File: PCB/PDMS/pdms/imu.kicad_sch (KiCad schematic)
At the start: 1 part

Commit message: Full imu schematics
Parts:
- added C? (x2): 100nF, symbol Device:C_Small
- added C?: 10nF, symbol Device:C_Small
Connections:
- net GND: now also IC?.2 (RES_1), IC?.3 (RES_2), C?.1, C?.2, C?.2
- net IMU_I2C_SA0: now reaches IC?.1 (SDO/SA0)
- net IMU_MODE_SEL: now reaches IC?.12 (CS)
- net IMU_SCL: now reaches IC?.13 (SCL)
- net IMU_I2C_SDA: now reaches IC?.14 (SDA)
- net IMU_INT1: now reaches IC?.4 (INT1)
- net +3.3V: now reaches IC?.5 (VDDIO)
- net +3.3V: now also IC?.8 (VDD), C?.1, C?.1, C?.2
- net IMU_INT2: now reaches IC?.9 (INT2)
- no-connect marks 0 -> 2
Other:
- note added: "ASM330 - SAFETY IMU"
- moved on the sheet: IC?

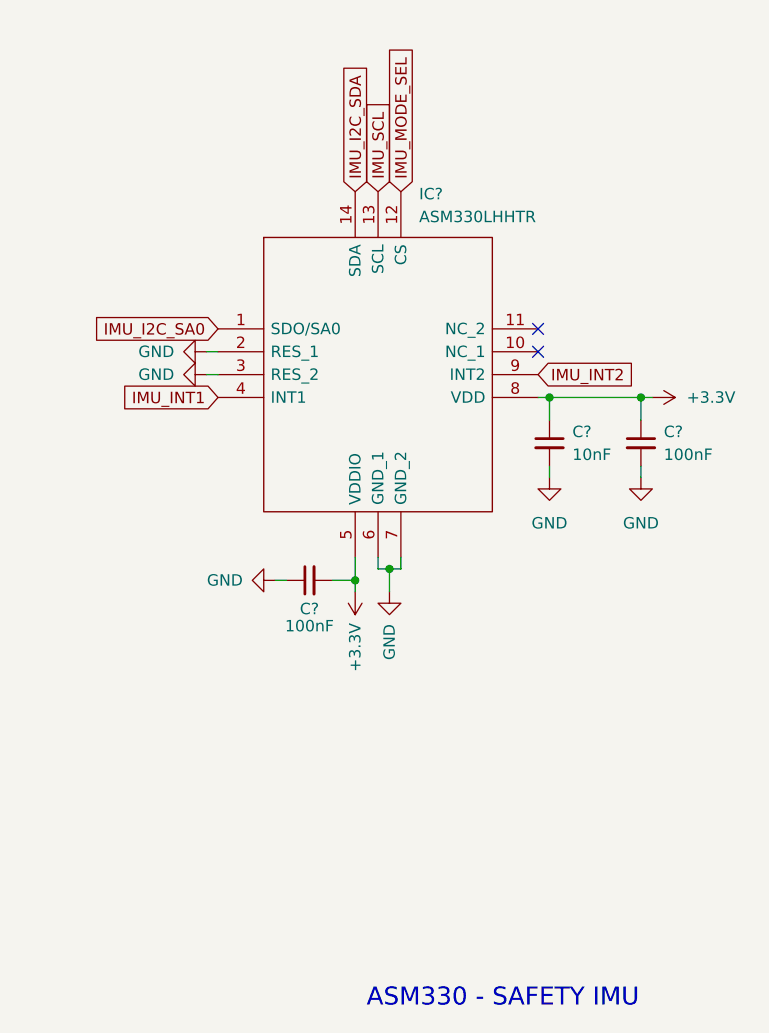
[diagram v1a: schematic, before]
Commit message: Modified power switch section - partly finished
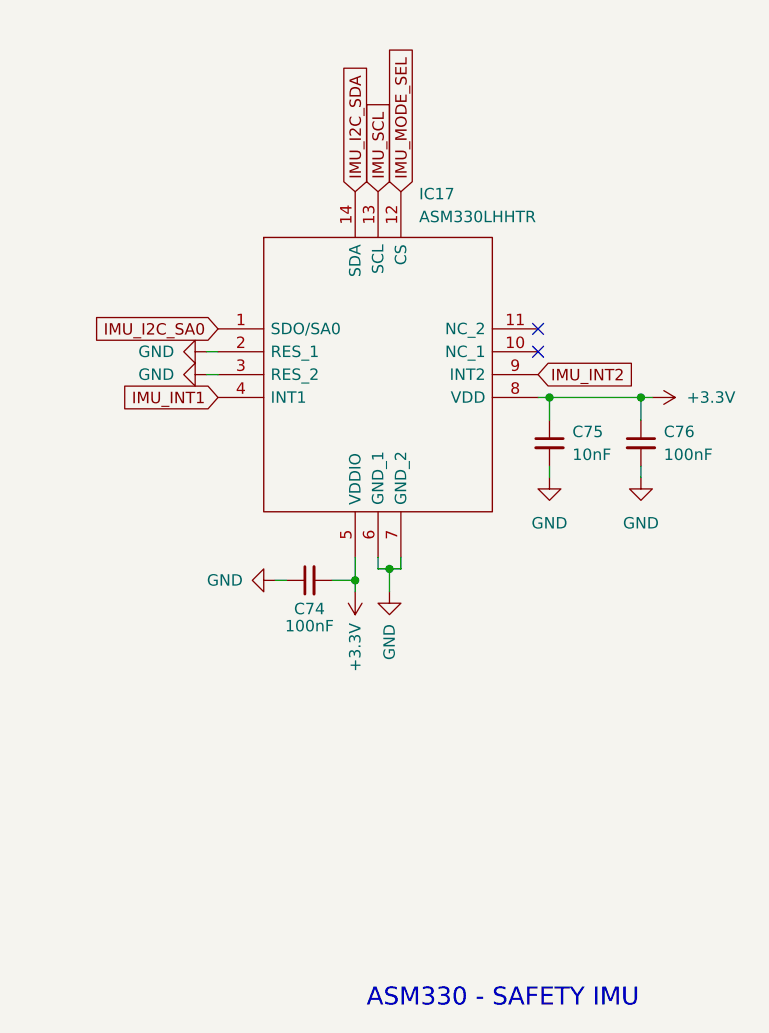
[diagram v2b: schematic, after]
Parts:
- gave numbers to parts that had none: 4
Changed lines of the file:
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@@
   (symbol (lib_id "power:GND") (at 130.175 69.85 0) (unit 1)
     (in_bom yes) (on_board yes) (fields_autoplaced)
-    (property "Reference" "#PWR?" (id 0) (at 130.175 76.2 0)
+    (property "Reference" "#PWR0293" (id 0) (at 130.175 76.2 0)
       (effects (font (size 1.27 1.27)) hide)
     )
@@
   (symbol (lib_id "Device:C_Small") (at 130.175 66.04 0) (unit 1)
     (in_bom yes) (on_board yes) (fields_autoplaced)
-    (property "Reference" "C?" (id 0) (at 132.715 64.7762 0)
+    (property "Reference" "C76" (id 0) (at 132.715 64.7762 0)
       (effects (font (size 1.27 1.27)) (justify left))
     )
@@
   (symbol (lib_id "Device:C_Small") (at 120.015 66.04 0) (unit 1)
     (in_bom yes) (on_board yes) (fields_autoplaced)
-    (property "Reference" "C?" (id 0) (at 122.555 64.7762 0)
+    (property "Reference" "C75" (id 0) (at 122.555 64.7762 0)
       (effects (font (size 1.27 1.27)) (justify left))
     )
@@
   (symbol (lib_id "power:+3.3V") (at 98.425 82.55 180) (unit 1)
     (in_bom yes) (on_board yes)
-    (property "Reference" "#PWR?" (id 0) (at 98.425 78.74 0)
+    (property "Reference" "#PWR0297" (id 0) (at 98.425 78.74 0)
       (effects (font (size 1.27 1.27)) hide)
     )
@@
   (symbol (lib_id "power:GND") (at 120.015 69.85 0) (unit 1)
     (in_bom yes) (on_board yes) (fields_autoplaced)
-    (property "Reference" "#PWR?" (id 0) (at 120.015 76.2 0)
+    (property "Reference" "#PWR0291" (id 0) (at 120.015 76.2 0)
       (effects (font (size 1.27 1.27)) hide)
     )
@@
   (symbol (lib_id "pdms_additional:ASM330LHHTR") (at 83.185 53.34 0) (unit 1)
     (in_bom yes) (on_board yes) (fields_autoplaced)
-    (property "Reference" "IC?" (id 0) (at 105.5244 38.354 0)
+    (property "Reference" "IC17" (id 0) (at 105.5244 38.354 0)
       (effects (font (size 1.27 1.27)) (justify left))
     )
@@
   (symbol (lib_id "power:GND") (at 81.915 58.42 270) (unit 1)
     (in_bom yes) (on_board yes)
-    (property "Reference" "#PWR?" (id 0) (at 75.565 58.42 0)
+    (property "Reference" "#PWR0294" (id 0) (at 75.565 58.42 0)
       (effects (font (size 1.27 1.27)) hide)
     )
@@
   (symbol (lib_id "Device:C_Small") (at 93.345 81.28 90) (unit 1)
     (in_bom yes) (on_board yes)
-    (property "Reference" "C?" (id 0) (at 93.345 84.455 90))
+    (property "Reference" "C74" (id 0) (at 93.345 84.455 90))
     (property "Value" "100nF" (id 1) (at 93.345 86.36 90))
     (property "Footprint" "" (id 2) (at 93.345 81.28 0)
@@
   (symbol (lib_id "power:GND") (at 89.535 81.28 270) (unit 1)
     (in_bom yes) (on_board yes)
-    (property "Reference" "#PWR?" (id 0) (at 83.185 81.28 0)
+    (property "Reference" "#PWR0298" (id 0) (at 83.185 81.28 0)
       (effects (font (size 1.27 1.27)) hide)
     )
@@
   (symbol (lib_id "power:GND") (at 102.235 82.55 0) (unit 1)
     (in_bom yes) (on_board yes)
-    (property "Reference" "#PWR?" (id 0) (at 102.235 88.9 0)
+    (property "Reference" "#PWR0296" (id 0) (at 102.235 88.9 0)
       (effects (font (size 1.27 1.27)) hide)
     )
@@
   (symbol (lib_id "power:+3.3V") (at 131.445 60.96 270) (unit 1)
     (in_bom yes) (on_board yes) (fields_autoplaced)
-    (property "Reference" "#PWR?" (id 0) (at 127.635 60.96 0)
+    (property "Reference" "#PWR0292" (id 0) (at 127.635 60.96 0)
       (effects (font (size 1.27 1.27)) hide)
     )
@@
   (symbol (lib_id "power:GND") (at 81.915 55.88 270) (unit 1)
     (in_bom yes) (on_board yes)
-    (property "Reference" "#PWR?" (id 0) (at 75.565 55.88 0)
-      (effects (font (size 1.27 1.27)) hide)
-    )
+    (property "Reference" "#PWR0295" (id 0) (at 75.565 55.88 0)
+      (effects (font (size 1.27 1.27)) hide)
+    )
